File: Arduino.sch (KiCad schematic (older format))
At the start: 17 parts

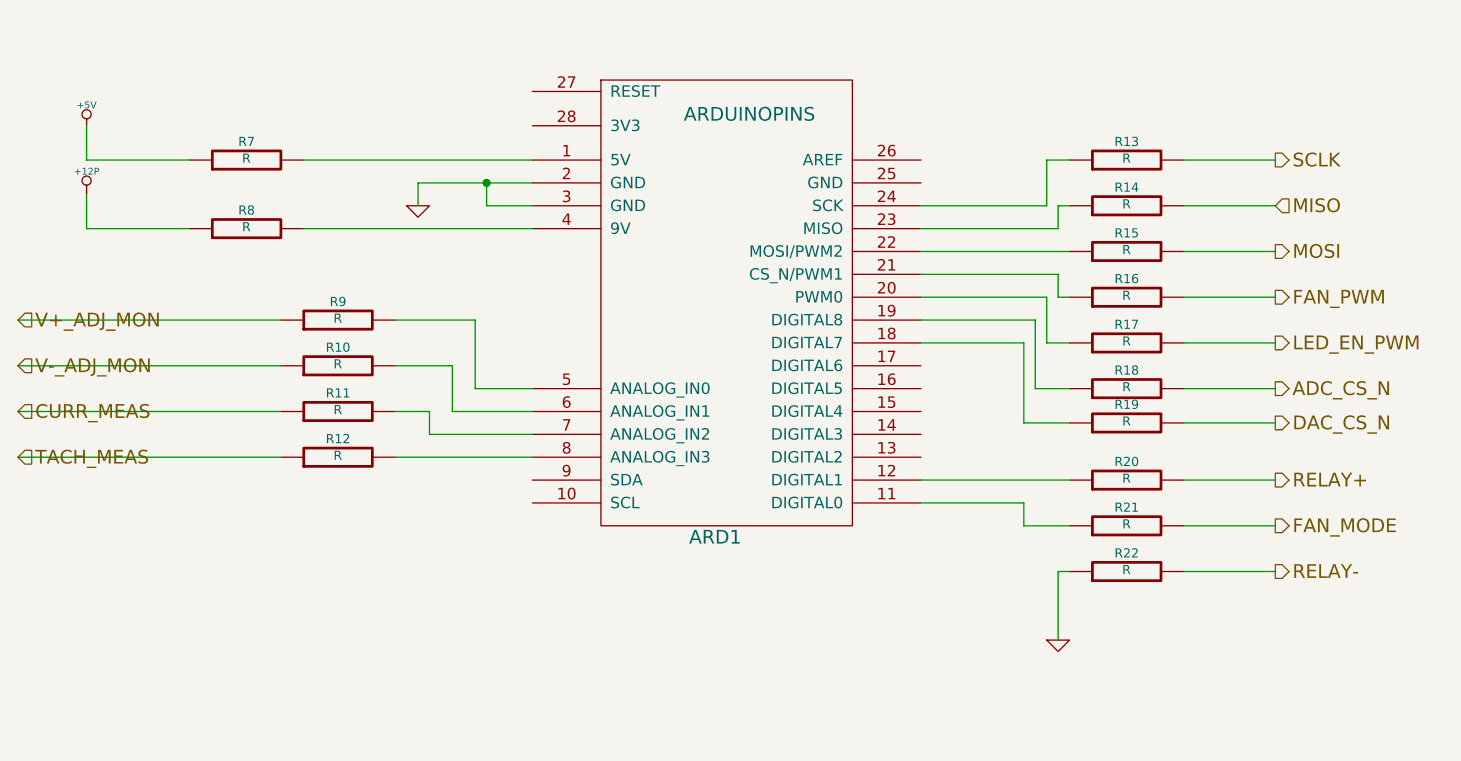
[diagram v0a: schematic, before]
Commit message: THERMOCOUPLE 02-22-2014
Associated and placed PCB footprints of thermocouple modules in layout
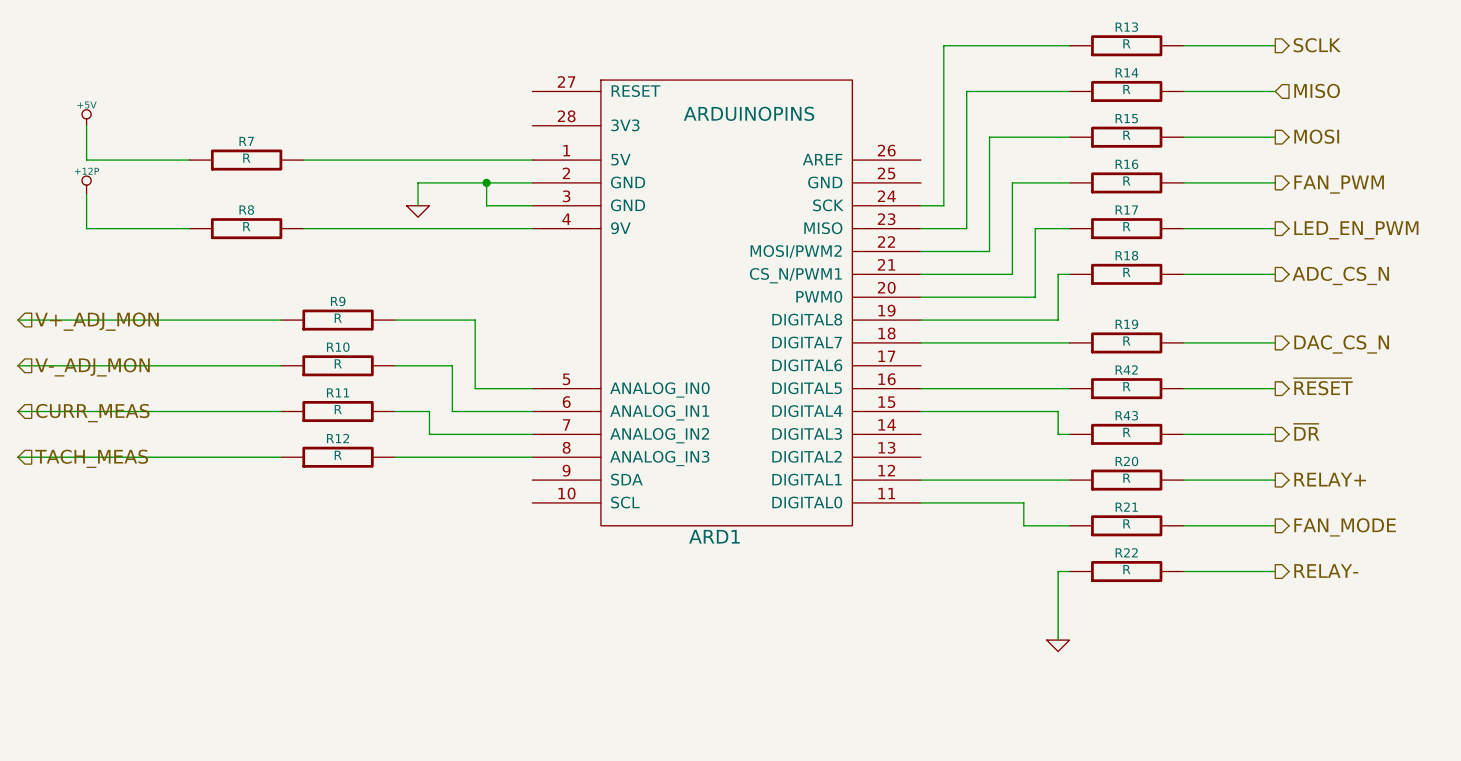
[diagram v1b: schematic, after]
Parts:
- added R42, R43: R, ~, symbol R
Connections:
- net at ARD1.15 (DIGITAL4): now also R43.1
- net at ARD1.16 (DIGITAL5): now also R42.1
- new net ~DR: R43.2
- new net ~RESET: R42.2
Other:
- moved on the sheet: R13, R14, R15, R16, R17, R18, R19
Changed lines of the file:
@@
 Sheet 2 9
 Title ""
-Date "20 feb 2014"
+Date "23 feb 2014"
 Rev ""
 Comp ""
@@
 Text HLabel 7000 3750 2    60   Output ~ 0
 RELAY-
-Text HLabel 7000 2350 2    60   Output ~ 0
+Text HLabel 7000 1850 2    60   Output ~ 0
 MOSI
-Text HLabel 7000 2150 2    60   Input ~ 0
+Text HLabel 7000 1650 2    60   Input ~ 0
 MISO
-Text HLabel 7000 1950 2    60   Output ~ 0
+Text HLabel 7000 1450 2    60   Output ~ 0
 SCLK
-Text HLabel 7000 3100 2    60   Output ~ 0
+Text HLabel 7000 2750 2    60   Output ~ 0
 DAC_CS_N
-Text HLabel 7000 2750 2    60   Output ~ 0
+Text HLabel 7000 2250 2    60   Output ~ 0
 LED_EN_PWM
-Text HLabel 7000 2550 2    60   Output ~ 0
+Text HLabel 7000 2050 2    60   Output ~ 0
 FAN_PWM
 Text HLabel 1500 3250 2    60   Input ~ 0
@@
 L R R16
 U 1 1 52F8B0F4
-P 6350 2550
-F 0 "R16" V 6430 2550 40  0000 C CNN
-F 1 "R" V 6357 2551 40  0000 C CNN
-F 2 "~" V 6280 2550 30  0000 C CNN
-F 3 "~" H 6350 2550 30  0000 C CNN
-	1    6350 2550
+P 6350 2050
+F 0 "R16" V 6430 2050 40  0000 C CNN
+F 1 "R" V 6357 2051 40  0000 C CNN
+F 2 "~" V 6280 2050 30  0000 C CNN
+F 3 "~" H 6350 2050 30  0000 C CNN
+	1    6350 2050
 	0    -1   -1   0
 $EndComp
@@
 $EndComp
 $Comp
-L GND #PWR4
+L GND #PWR01
 U 1 1 52F8B714
 P 6050 4050
-F 0 "#PWR4" H 6050 4050 30  0001 C CNN
+F 0 "#PWR01" H 6050 4050 30  0001 C CNN
 F 1 "GND" H 6050 3980 30  0001 C CNN
 F 2 "" H 6050 4050 60  0000 C CNN
@@
 L R R19
 U 1 1 52F8BF34
-P 6350 3100
-F 0 "R19" V 6430 3100 40  0000 C CNN
-F 1 "R" V 6357 3101 40  0000 C CNN
-F 2 "~" V 6280 3100 30  0000 C CNN
-F 3 "~" H 6350 3100 30  0000 C CNN
-	1    6350 3100
+P 6350 2750
+F 0 "R19" V 6430 2750 40  0000 C CNN
+F 1 "R" V 6357 2751 40  0000 C CNN
+F 2 "~" V 6280 2750 30  0000 C CNN
+F 3 "~" H 6350 2750 30  0000 C CNN
+	1    6350 2750
 	0    -1   -1   0
 $EndComp
@@
 L R R15
 U 1 1 52F8BF4E
-P 6350 2350
-F 0 "R15" V 6430 2350 40  0000 C CNN
-F 1 "R" V 6357 2351 40  0000 C CNN
-F 2 "~" V 6280 2350 30  0000 C CNN
-F 3 "~" H 6350 2350 30  0000 C CNN
-	1    6350 2350
+P 6350 1850
+F 0 "R15" V 6430 1850 40  0000 C CNN
+F 1 "R" V 6357 1851 40  0000 C CNN
+F 2 "~" V 6280 1850 30  0000 C CNN
+F 3 "~" H 6350 1850 30  0000 C CNN
+	1    6350 1850
 	0    -1   -1   0
 $EndComp
@@
 L R R14
 U 1 1 52F8BF54
-P 6350 2150
-F 0 "R14" V 6430 2150 40  0000 C CNN
-F 1 "R" V 6357 2151 40  0000 C CNN
-F 2 "~" V 6280 2150 30  0000 C CNN
-F 3 "~" H 6350 2150 30  0000 C CNN
-	1    6350 2150
+P 6350 1650
+F 0 "R14" V 6430 1650 40  0000 C CNN
+F 1 "R" V 6357 1651 40  0000 C CNN
+F 2 "~" V 6280 1650 30  0000 C CNN
+F 3 "~" H 6350 1650 30  0000 C CNN
+	1    6350 1650
 	0    -1   -1   0
 $EndComp
@@
 L R R13
 U 1 1 52F8BF5A
-P 6350 1950
-F 0 "R13" V 6430 1950 40  0000 C CNN
-F 1 "R" V 6357 1951 40  0000 C CNN
-F 2 "~" V 6280 1950 30  0000 C CNN
-F 3 "~" H 6350 1950 30  0000 C CNN
-	1    6350 1950
-	0    -1   -1   0
-$EndComp
-Wire Wire Line
-	5450 2450 6050 2450
+P 6350 1450
+F 0 "R13" V 6430 1450 40  0000 C CNN
+F 1 "R" V 6357 1451 40  0000 C CNN
+F 2 "~" V 6280 1450 30  0000 C CNN
+F 3 "~" H 6350 1450 30  0000 C CNN
+	1    6350 1450
+	0    -1   -1   0
+$EndComp
+Wire Wire Line
+	5450 2450 5850 2450
 Wire Wire Line
 	5450 3350 6100 3350
@@
 	6600 3350 7000 3350
 Wire Wire Line
-	6600 2550 7000 2550
+	6600 2050 7000 2050
 Wire Wire Line
 	6600 3750 7000 3750
@@
 	1500 2650 2650 2650
 Wire Wire Line
-	7000 3100 6600 3100
-Wire Wire Line
-	7000 2350 6600 2350
-Wire Wire Line
-	7000 2150 6600 2150
-Wire Wire Line
-	7000 1950 6600 1950
-Wire Wire Line
-	5900 3100 6100 3100
-Wire Wire Line
-	5450 2350 6100 2350
-Wire Wire Line
-	5450 2250 6050 2250
-Wire Wire Line
-	6050 2250 6050 2150
-Wire Wire Line
-	6050 2150 6100 2150
-Wire Wire Line
-	5450 2150 6000 2150
-Wire Wire Line
-	6000 2150 6000 1950
-Wire Wire Line
-	6000 1950 6100 1950
+	7000 2750 6600 2750
+Wire Wire Line
+	7000 1850 6600 1850
+Wire Wire Line
+	7000 1650 6600 1650
+Wire Wire Line
+	7000 1450 6600 1450
+Wire Wire Line
+	5450 2350 5750 2350
+Wire Wire Line
+	5450 2250 5650 2250
+Wire Wire Line
+	5650 2250 5650 1650
+Wire Wire Line
+	5650 1650 6100 1650
+Wire Wire Line
+	5450 2150 5550 2150
+Wire Wire Line
+	5550 2150 5550 1450
+Wire Wire Line
+	5550 1450 6100 1450
 $Comp
 L R R22
@@
 L R R17
 U 1 1 52F8C429
-P 6350 2750
-F 0 "R17" V 6430 2750 40  0000 C CNN
-F 1 "R" V 6357 2751 40  0000 C CNN
-F 2 "~" V 6280 2750 30  0000 C CNN
-F 3 "~" H 6350 2750 30  0000 C CNN
-	1    6350 2750
-	0    -1   -1   0
-$EndComp
-Wire Wire Line
-	7000 2750 6600 2750
-Wire Wire Line
-	5450 2550 6000 2550
-Wire Wire Line
-	6000 2550 6000 2750
-Wire Wire Line
-	6000 2750 6100 2750
-Text HLabel 7000 2950 2    60   Output ~ 0
+P 6350 2250
+F 0 "R17" V 6430 2250 40  0000 C CNN
+F 1 "R" V 6357 2251 40  0000 C CNN
+F 2 "~" V 6280 2250 30  0000 C CNN
+F 3 "~" H 6350 2250 30  0000 C CNN
+	1    6350 2250
+	0    -1   -1   0
+$EndComp
+Wire Wire Line
+	7000 2250 6600 2250
+Wire Wire Line
+	5450 2550 5950 2550
+Text HLabel 7000 2450 2    60   Output ~ 0
 ADC_CS_N
 $Comp
 L R R18
 U 1 1 52F912F6
-P 6350 2950
-F 0 "R18" V 6430 2950 40  0000 C CNN
-F 1 "R" V 6357 2951 40  0000 C CNN
-F 2 "~" V 6280 2950 30  0000 C CNN
-F 3 "~" H 6350 2950 30  0000 C CNN
-	1    6350 2950
-	0    -1   -1   0
-$EndComp
-Wire Wire Line
-	7000 2950 6600 2950
-Wire Wire Line
-	5450 2650 5950 2650
-Wire Wire Line
-	5950 2650 5950 2950
-Wire Wire Line
-	5950 2950 6100 2950
-Wire Wire Line
-	5900 3100 5900 2750
-Wire Wire Line
-	5900 2750 5450 2750
-Wire Wire Line
-	6050 2550 6100 2550
-Wire Wire Line
-	6050 2450 6050 2550
+P 6350 2450
+F 0 "R18" V 6430 2450 40  0000 C CNN
+F 1 "R" V 6357 2451 40  0000 C CNN
+F 2 "~" V 6280 2450 30  0000 C CNN
+F 3 "~" H 6350 2450 30  0000 C CNN
+	1    6350 2450
+	0    -1   -1   0
+$EndComp
+Wire Wire Line
+	7000 2450 6600 2450
+Wire Wire Line
+	5450 2650 6050 2650
+Wire Wire Line
+	5450 2750 6100 2750
+Wire Wire Line
+	5850 2050 6100 2050
+Wire Wire Line
+	5850 2450 5850 2050
 Text HLabel 7000 3550 2    60   Output ~ 0
 FAN_MODE
@@
 	1800 2250 1800 2100
 $Comp
-L +12P #PWR2
+L +12P #PWR02
 U 1 1 52F9FFAF
 P 1800 2100
-F 0 "#PWR2" H 1800 2070 30  0001 C CNN
+F 0 "#PWR02" H 1800 2070 30  0001 C CNN
 F 1 "+12P" H 1800 2200 30  0000 C CNN
 F 2 "" H 1800 2100 60  0000 C CNN
@@
 	1800 1950 1800 1800
 $Comp
-L +5V #PWR1
+L +5V #PWR03
 U 1 1 5302EB20
 P 1800 1800
-F 0 "#PWR1" H 1800 1890 20  0001 C CNN
+F 0 "#PWR03" H 1800 1890 20  0001 C CNN
 F 1 "+5V" H 1800 1890 30  0000 C CNN
 F 2 "" H 1800 1800 60  0000 C CNN
@@
 $EndComp
 Wire Wire Line
-	3750 2050 3250 2050
+	3250 2050 3750 2050
 Wire Wire Line
 	3750 2150 3550 2150
@@
 Connection ~ 3550 2050
 $Comp
-L GND #PWR3
+L GND #PWR04
 U 1 1 5302EB9F
 P 3250 2150
-F 0 "#PWR3" H 3250 2150 30  0001 C CNN
+F 0 "#PWR04" H 3250 2150 30  0001 C CNN
 F 1 "GND" H 3250 2080 30  0001 C CNN
 F 2 "" H 3250 2150 60  0000 C CNN
@@
 Wire Wire Line
 	3250 2050 3250 2150
+Wire Wire Line
+	5750 2350 5750 1850
+Wire Wire Line
+	5750 1850 6100 1850
+Wire Wire Line
+	5950 2550 5950 2250
+Wire Wire Line
+	5950 2250 6100 2250
+Wire Wire Line
+	6050 2650 6050 2450
+Wire Wire Line
+	6050 2450 6100 2450
+Text HLabel 7000 2950 2    60   Output ~ 0
+~RESET
+$Comp
+L R R42
+U 1 1 5309B121
+P 6350 2950
+F 0 "R42" V 6430 2950 40  0000 C CNN
+F 1 "R" V 6357 2951 40  0000 C CNN
+F 2 "~" V 6280 2950 30  0000 C CNN
+F 3 "~" H 6350 2950 30  0000 C CNN
+	1    6350 2950
+	0    -1   -1   0
+$EndComp
+Wire Wire Line
+	7000 2950 6600 2950
+Text HLabel 7000 3150 2    60   Output ~ 0
+~DR
+$Comp
+L R R43
+U 1 1 5309B129
+P 6350 3150
+F 0 "R43" V 6430 3150 40  0000 C CNN
+F 1 "R" V 6357 3151 40  0000 C CNN
+F 2 "~" V 6280 3150 30  0000 C CNN
+F 3 "~" H 6350 3150 30  0000 C CNN
+	1    6350 3150
+	0    -1   -1   0
+$EndComp
+Wire Wire Line
+	7000 3150 6600 3150
+Wire Wire Line
+	6100 2950 5450 2950
+Wire Wire Line
+	5450 3050 6050 3050
+Wire Wire Line
+	6050 3050 6050 3150
+Wire Wire Line
+	6050 3150 6100 3150
 $EndSCHEMATC

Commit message: Fan Controller Module
1) Created and associated the footprints of fan controller module
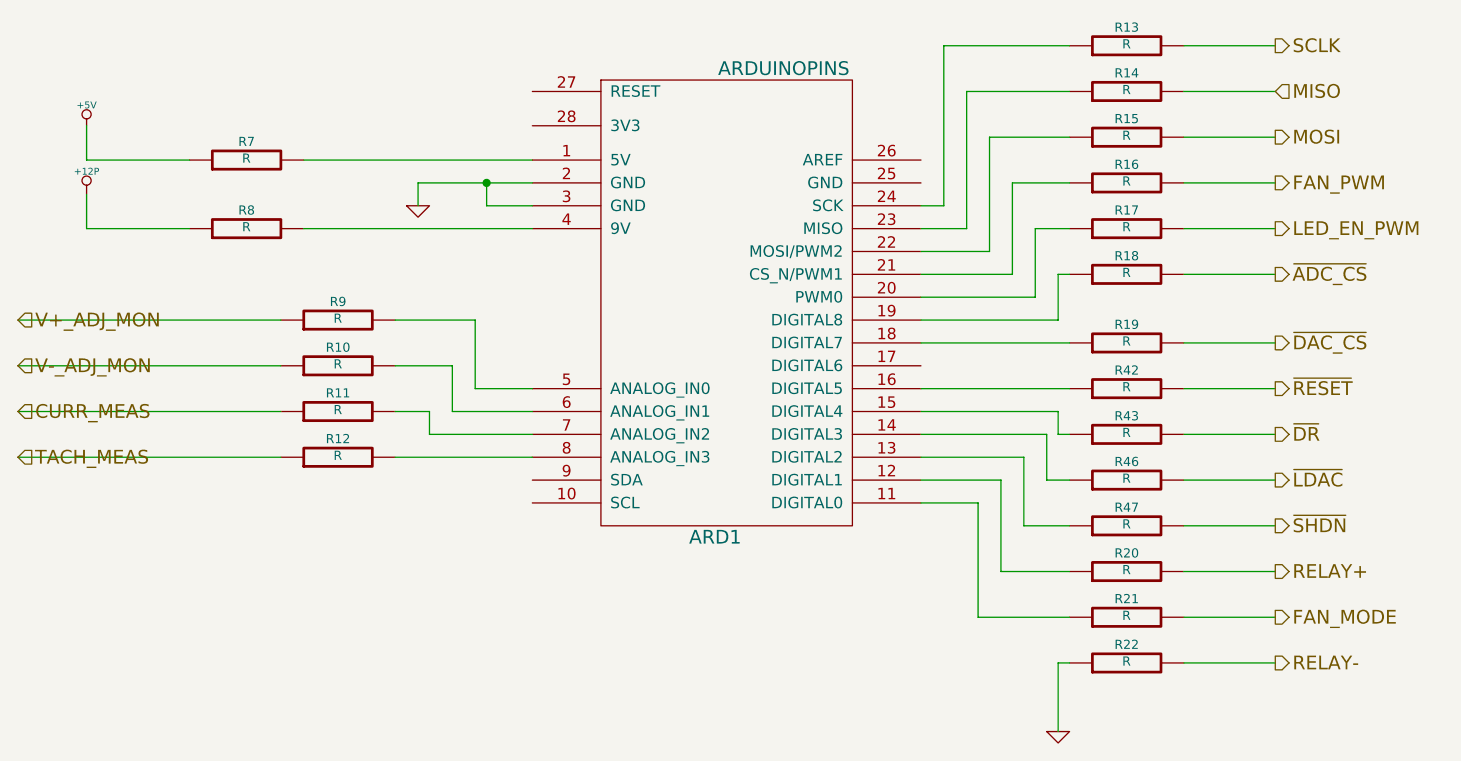
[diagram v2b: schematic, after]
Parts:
- added R46, R47: R, ~, symbol R
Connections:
- net at ARD1.13 (DIGITAL2): now also R47.1
- net at ARD1.14 (DIGITAL3): now also R46.1
- net ADC_CS_N renamed ~ADC_CS
- net DAC_CS_N renamed ~DAC_CS
- new net ~LDAC: R46.2
- new net ~SHDN: R47.2
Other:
- moved on the sheet: R20, R21, R22
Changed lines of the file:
@@
 Sheet 2 9
 Title ""
-Date "23 feb 2014"
+Date "24 feb 2014"
 Rev ""
 Comp ""
@@
 Comment4 ""
 $EndDescr
-Text HLabel 7000 3350 2    60   Output ~ 0
+Text HLabel 7000 3750 2    60   Output ~ 0
 RELAY+
-Text HLabel 7000 3750 2    60   Output ~ 0
+Text HLabel 7000 4150 2    60   Output ~ 0
 RELAY-
 Text HLabel 7000 1850 2    60   Output ~ 0
@@
 SCLK
 Text HLabel 7000 2750 2    60   Output ~ 0
-DAC_CS_N
+~DAC_CS
 Text HLabel 7000 2250 2    60   Output ~ 0
 LED_EN_PWM
@@
 L R R20
 U 1 1 52F8B683
-P 6350 3350
-F 0 "R20" V 6430 3350 40  0000 C CNN
-F 1 "R" V 6357 3351 40  0000 C CNN
-F 2 "~" V 6280 3350 30  0000 C CNN
-F 3 "~" H 6350 3350 30  0000 C CNN
-	1    6350 3350
+P 6350 3750
+F 0 "R20" V 6430 3750 40  0000 C CNN
+F 1 "R" V 6357 3751 40  0000 C CNN
+F 2 "~" V 6280 3750 30  0000 C CNN
+F 3 "~" H 6350 3750 30  0000 C CNN
+	1    6350 3750
 	0    -1   -1   0
 $EndComp
@@
 L GND #PWR01
 U 1 1 52F8B714
-P 6050 4050
-F 0 "#PWR01" H 6050 4050 30  0001 C CNN
-F 1 "GND" H 6050 3980 30  0001 C CNN
-F 2 "" H 6050 4050 60  0000 C CNN
-F 3 "" H 6050 4050 60  0000 C CNN
-	1    6050 4050
+P 6050 4450
+F 0 "#PWR01" H 6050 4450 30  0001 C CNN
+F 1 "GND" H 6050 4380 30  0001 C CNN
+F 2 "" H 6050 4450 60  0000 C CNN
+F 3 "" H 6050 4450 60  0000 C CNN
+	1    6050 4450
 	1    0    0    -1
 $EndComp
@@
 	5450 2450 5850 2450
 Wire Wire Line
-	5450 3350 6100 3350
-Wire Wire Line
-	6600 3350 7000 3350
+	5450 3350 5800 3350
+Wire Wire Line
+	6600 3750 7000 3750
 Wire Wire Line
 	6600 2050 7000 2050
 Wire Wire Line
-	6600 3750 7000 3750
-Wire Wire Line
-	6050 3750 6050 4050
+	6600 4150 7000 4150
+Wire Wire Line
+	6050 4150 6050 4450
 Wire Wire Line
 	3750 3250 3150 3250
@@
 L R R22
 U 1 1 52F8C0B1
-P 6350 3750
-F 0 "R22" V 6430 3750 40  0000 C CNN
-F 1 "R" V 6357 3751 40  0000 C CNN
-F 2 "~" V 6280 3750 30  0000 C CNN
-F 3 "~" H 6350 3750 30  0000 C CNN
-	1    6350 3750
-	0    -1   -1   0
-$EndComp
-Wire Wire Line
-	6100 3750 6050 3750
+P 6350 4150
+F 0 "R22" V 6430 4150 40  0000 C CNN
+F 1 "R" V 6357 4151 40  0000 C CNN
+F 2 "~" V 6280 4150 30  0000 C CNN
+F 3 "~" H 6350 4150 30  0000 C CNN
+	1    6350 4150
+	0    -1   -1   0
+$EndComp
+Wire Wire Line
+	6100 4150 6050 4150
 $Comp
 L R R17
@@
 	5450 2550 5950 2550
 Text HLabel 7000 2450 2    60   Output ~ 0
-ADC_CS_N
+~ADC_CS
 $Comp
 L R R18
@@
 Wire Wire Line
 	5850 2450 5850 2050
-Text HLabel 7000 3550 2    60   Output ~ 0
+Text HLabel 7000 3950 2    60   Output ~ 0
 FAN_MODE
 $Comp
 L R R21
 U 1 1 52F9FE44
-P 6350 3550
-F 0 "R21" V 6430 3550 40  0000 C CNN
-F 1 "R" V 6357 3551 40  0000 C CNN
-F 2 "~" V 6280 3550 30  0000 C CNN
-F 3 "~" H 6350 3550 30  0000 C CNN
-	1    6350 3550
-	0    -1   -1   0
-$EndComp
-Wire Wire Line
-	5900 3550 6100 3550
-Wire Wire Line
-	5450 3450 5900 3450
-Wire Wire Line
-	5900 3450 5900 3550
-Wire Wire Line
-	7000 3550 6600 3550
-$Comp
-L ARDUINOPINS ARD1
-U 1 1 52F9FF33
-P 4700 3350
-F 0 "ARD1" H 4550 3100 60  0000 C CNN
-F 1 "ARDUINOPINS" H 4700 4950 60  0000 C CNN
-F 2 "~" H 4700 3350 60  0000 C CNN
-F 3 "~" H 4700 3350 60  0000 C CNN
-	1    4700 3350
-	1    0    0    -1
-$EndComp
+P 6350 3950
+F 0 "R21" V 6430 3950 40  0000 C CNN
+F 1 "R" V 6357 3951 40  0000 C CNN
+F 2 "~" V 6280 3950 30  0000 C CNN
+F 3 "~" H 6350 3950 30  0000 C CNN
+	1    6350 3950
+	0    -1   -1   0
+$EndComp
+Wire Wire Line
+	5700 3950 6100 3950
+Wire Wire Line
+	5450 3450 5700 3450
+Wire Wire Line
+	5700 3450 5700 3950
+Wire Wire Line
+	7000 3950 6600 3950
 $Comp
 L R R8
@@
 Wire Wire Line
 	6050 3150 6100 3150
+$Comp
+L ARDUINOPINS ARD1
+U 1 1 530A9E5C
+P 4700 3350
+F 0 "ARD1" H 4550 3100 60  0000 C CNN
+F 1 "ARDUINOPINS" H 4850 5150 60  0000 C CNN
+F 2 "~" H 4700 3350 60  0000 C CNN
+F 3 "~" H 4700 3350 60  0000 C CNN
+	1    4700 3350
+	1    0    0    -1
+$EndComp
+Wire Wire Line
+	5800 3350 5800 3750
+Wire Wire Line
+	5800 3750 6100 3750
+$Comp
+L R R47
+U 1 1 530AF518
+P 6350 3550
+F 0 "R47" V 6430 3550 40  0000 C CNN
+F 1 "R" V 6357 3551 40  0000 C CNN
+F 2 "~" V 6280 3550 30  0000 C CNN
+F 3 "~" H 6350 3550 30  0000 C CNN
+	1    6350 3550
+	0    -1   -1   0
+$EndComp
+$Comp
+L R R46
+U 1 1 530AF51E
+P 6350 3350
+F 0 "R46" V 6430 3350 40  0000 C CNN
+F 1 "R" V 6357 3351 40  0000 C CNN
+F 2 "~" V 6280 3350 30  0000 C CNN
+F 3 "~" H 6350 3350 30  0000 C CNN
+	1    6350 3350
+	0    -1   -1   0
+$EndComp
+Wire Wire Line
+	5450 3250 5900 3250
+Wire Wire Line
+	5900 3250 5900 3550
+Wire Wire Line
+	5900 3550 6100 3550
+Wire Wire Line
+	5450 3150 6000 3150
+Wire Wire Line
+	6000 3150 6000 3350
+Wire Wire Line
+	6000 3350 6100 3350
+Wire Wire Line
+	6600 3350 7000 3350
+Wire Wire Line
+	6600 3550 7000 3550
+Text HLabel 7000 3350 2    60   Output ~ 0
+~LDAC
+Text HLabel 7000 3550 2    60   Output ~ 0
+~SHDN
 $EndSCHEMATC
